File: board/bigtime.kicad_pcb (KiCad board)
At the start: 2 copper layers, 90 x 142 mm, 122 parts, among them IC1 NPIC6C596A, IC2 TPS62152, IC3 25AA02E48, IC4 STM32F407VET6, IC5 KSZ8081RNx, IC6 MAX5969x, IC7 MAX17503, IC8 LDL212DR, J1 RJHSE-538B, J2 MICROUSB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

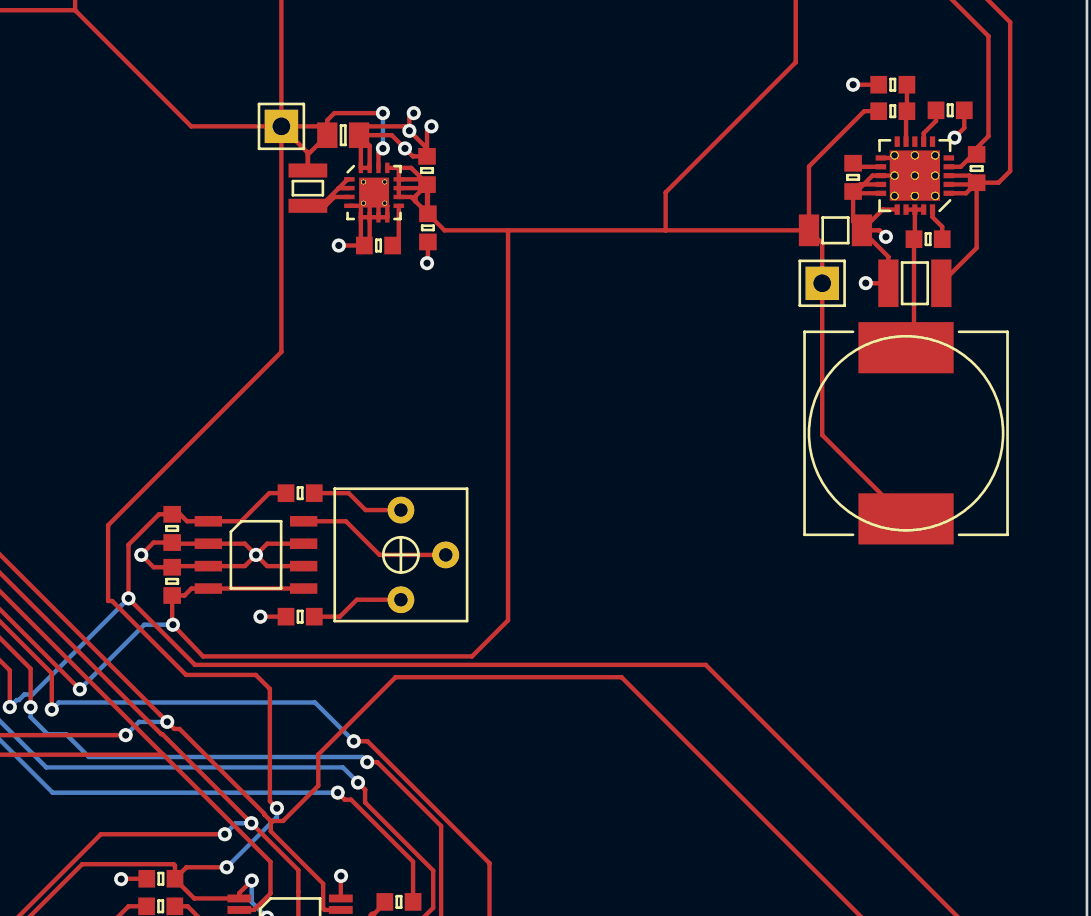
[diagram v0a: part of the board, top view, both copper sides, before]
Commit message: Tidied SMPS layouts
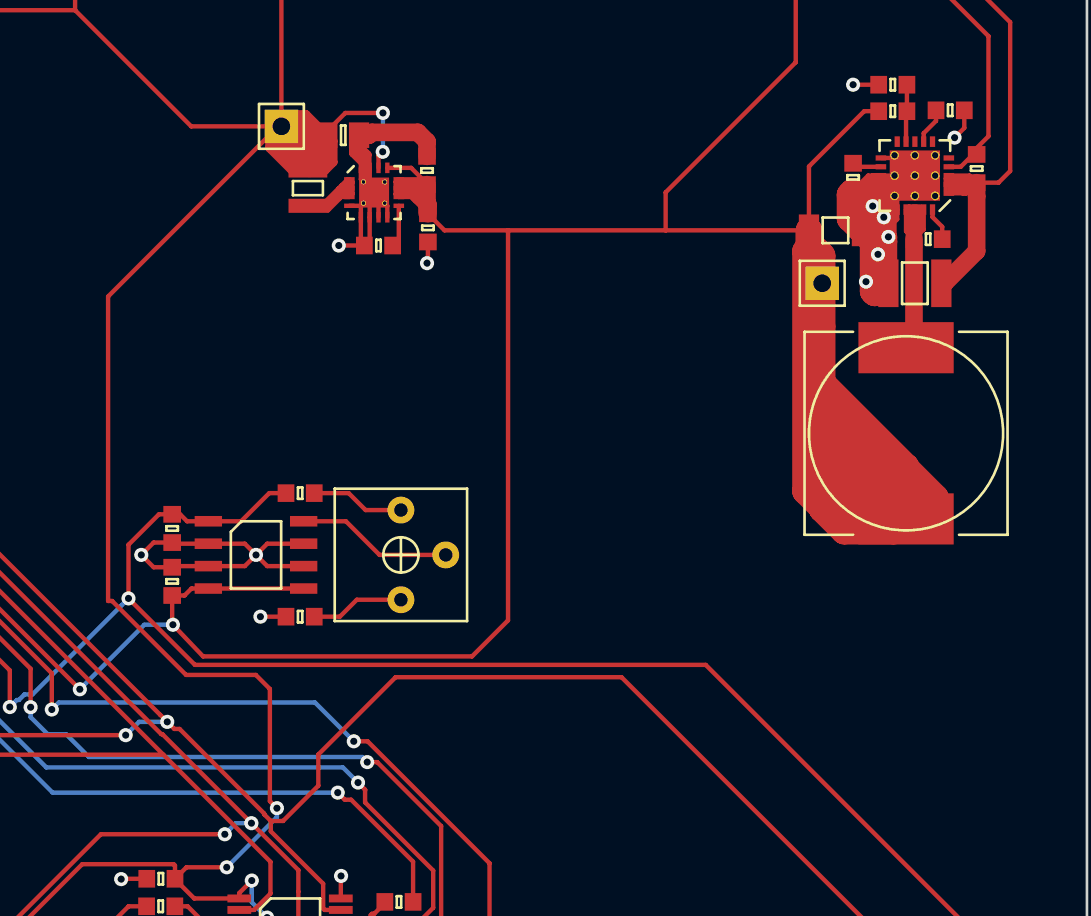
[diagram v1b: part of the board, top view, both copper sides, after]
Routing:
- net +12V: track 255.4 -> 314.3 mm
- net GND: track 155.6 -> 189.1 mm, vias 52 -> 51
- net +3V3: track 486.9 -> 500.6 mm
- net Net-(IC2-Pad1): track 6.13 -> 14.9 mm
- net Net-(C39-Pad2): track 9.03 -> 15.8 mm
- net +48V: track 82.6 -> 87.7 mm

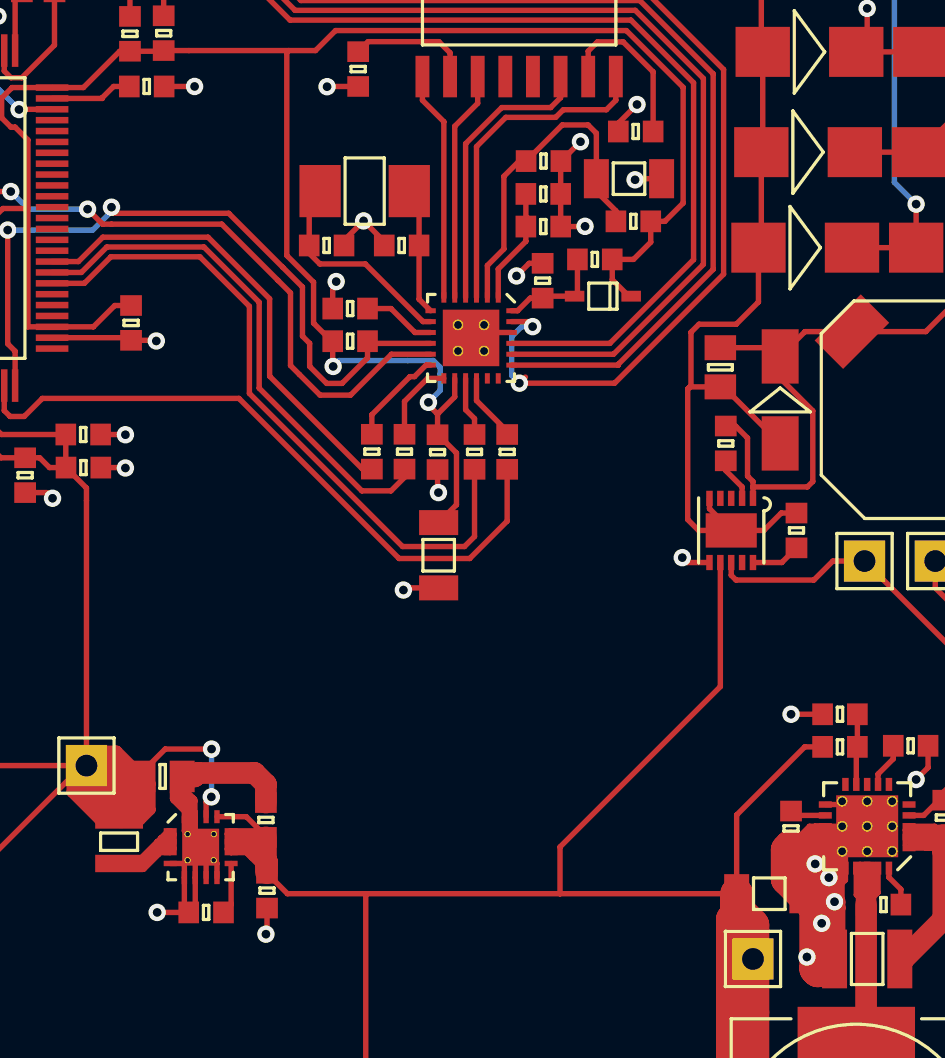
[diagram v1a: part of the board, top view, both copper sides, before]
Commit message: Made capacitors more consistent in vals+fps
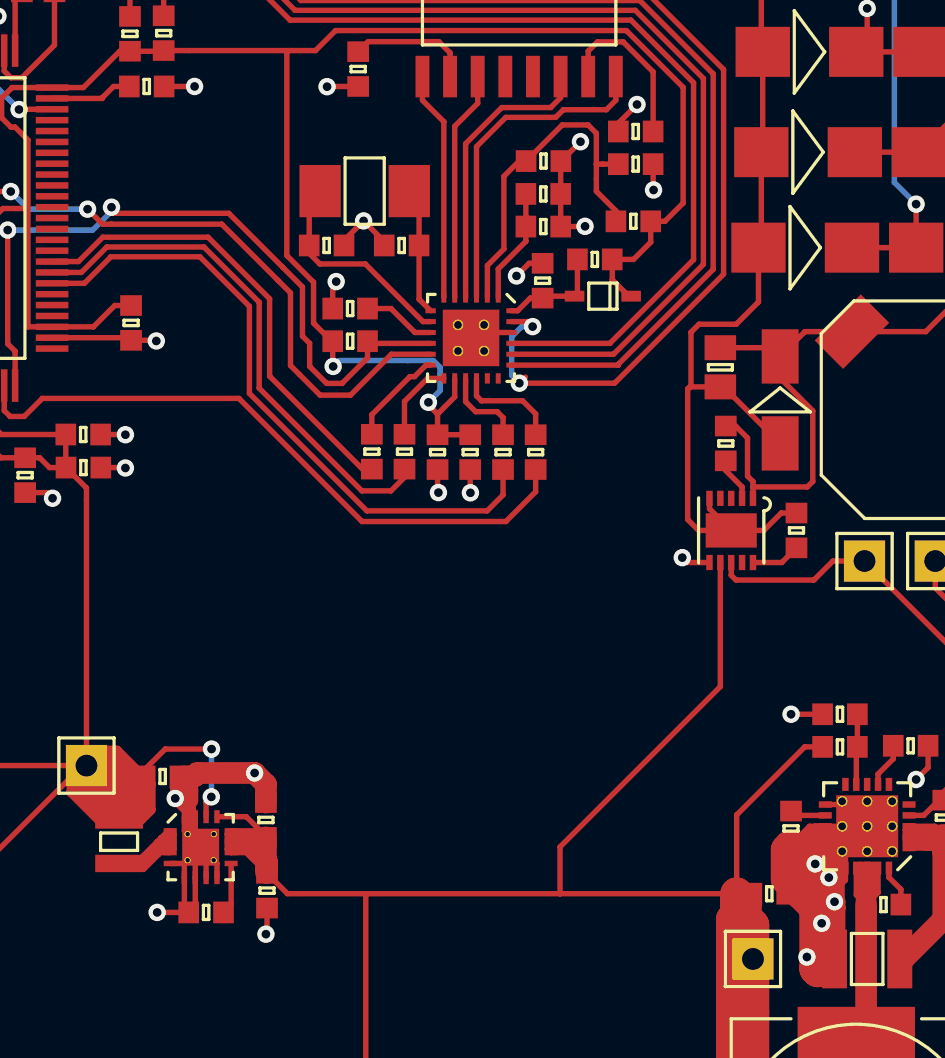
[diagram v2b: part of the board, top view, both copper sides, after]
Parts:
- C23, C25: footprint agg:1206 -> agg:0603
- C35: value C -> 10u
- C4: footprint agg:0805 -> agg:0603
- C41: value 2u -> 2u2; footprint agg:1206 -> agg:0603
- R24: value 3M3 -> 2M
- moved C25 4.96 mm to (187.0, 66.4)
- moved R13 1.31 mm to (188.5, 66.4)
- moved R14 1.31 mm to (190.0, 66.4)
- moved C23 0.74 mm to (194.6, 53.2)
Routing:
- net +3V3: track 500.6 -> 497.4 mm
- net +12V: track 314.3 -> 316.7 mm
- net Net-(IC5-Pad16): track 3.16 -> 4.82 mm
- net /RMII_CRS_DV: track 31.1 -> 29.9 mm
- net Net-(IC5-Pad15): track 2.75 -> 3.88 mm
- net Net-(C23-Pad1): track 15.9 -> 16.9 mm
- net GND: track 189.1 -> 190.1 mm, vias 51 -> 53
- net /RMII_REF_CLK: track 30.9 -> 30.0 mm

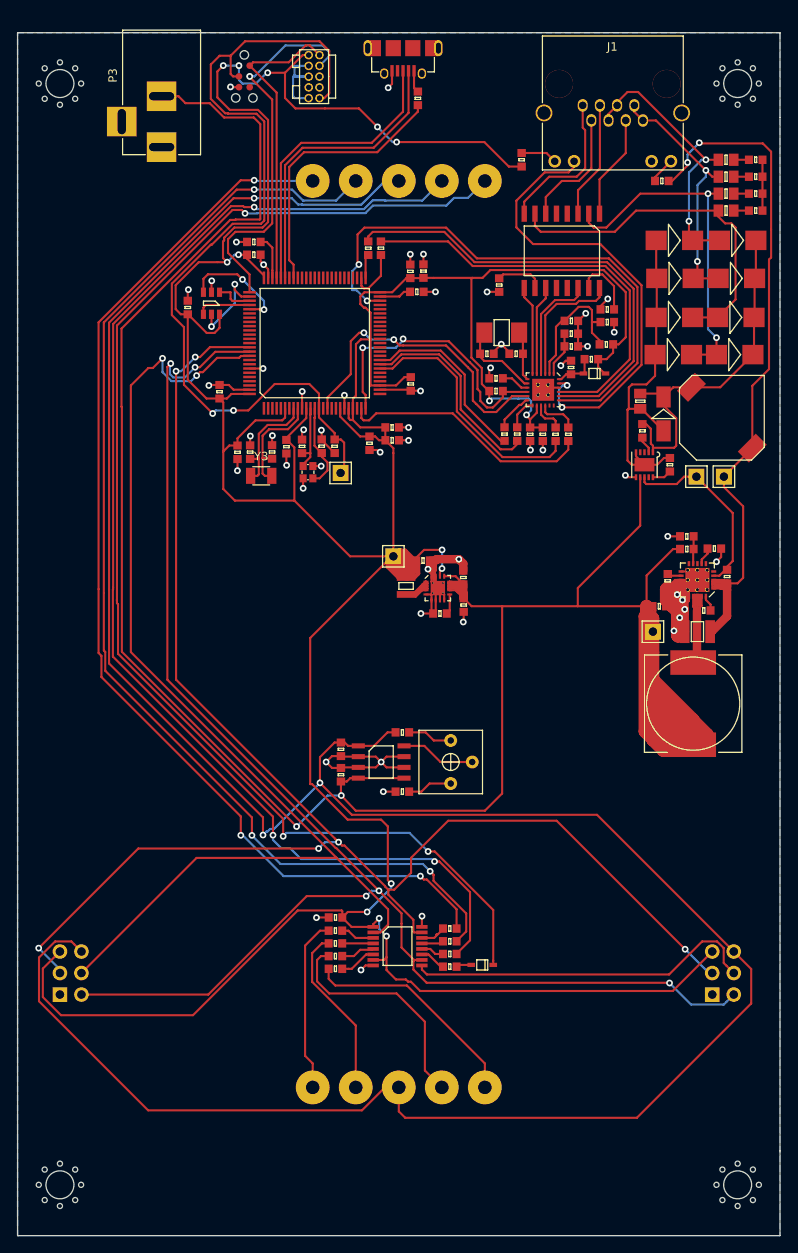
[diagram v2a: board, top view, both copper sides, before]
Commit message: Tidied top half of board
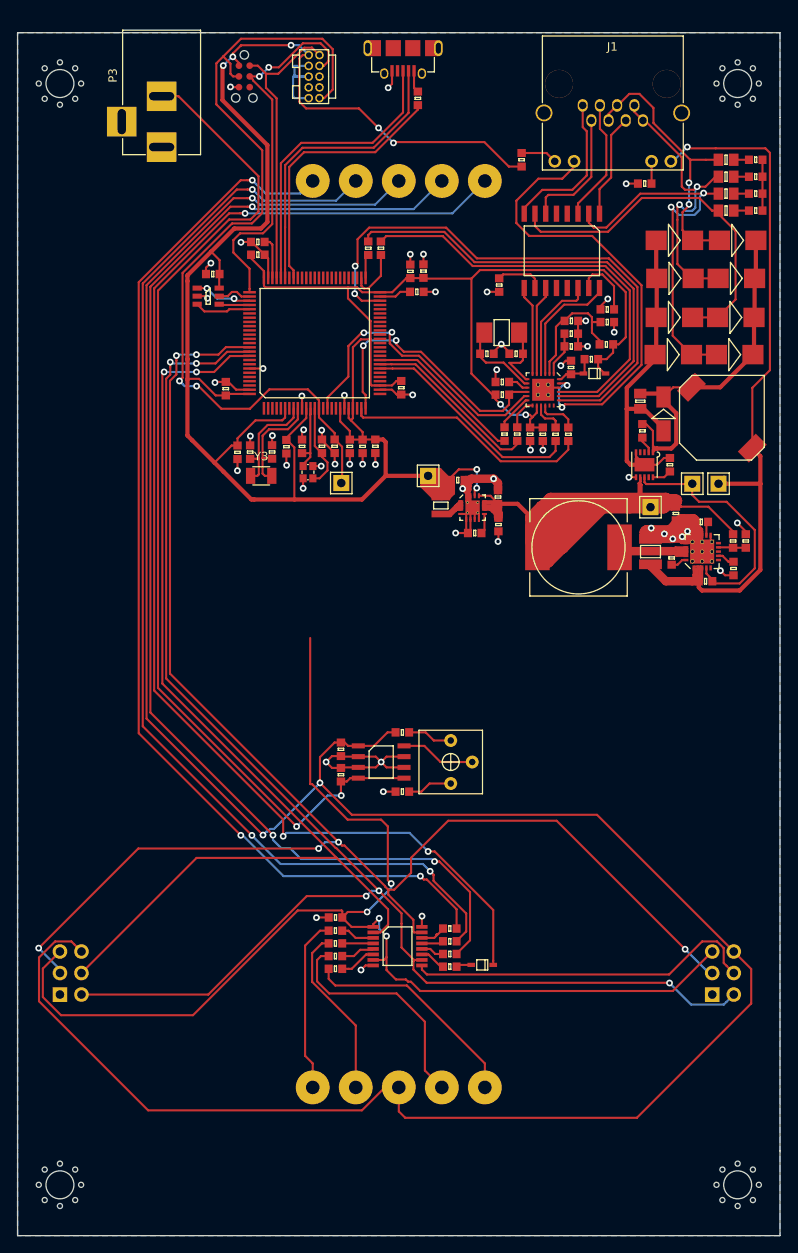
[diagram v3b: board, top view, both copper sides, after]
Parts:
- moved L4 22.9 mm to (191.2, 79.8), turned to 270 degrees
- moved TP4 14.7 mm to (199.7, 75.0), turned to 180 degrees
- moved C41 11.1 mm to (202.7, 75.8), turned to 270 degrees
- moved C38 11.0 mm to (199.7, 80.2), turned to 270 degrees
- moved C2 10.3 mm to (181.7, 73.8)
- moved C3 10.3 mm to (179.0, 78.1)
- moved C4 10.3 mm to (177.0, 71.8)
- moved C46 10.3 mm to (181.8, 77.1)
- moved IC2 10.3 mm to (178.7, 75.1)
- moved L1 10.3 mm to (175.0, 74.8)
- moved TP1 10.3 mm to (173.5, 71.3)
- moved C43 8.00 mm to (205.7, 76.8), turned to 180 degrees
- moved C39 7.27 mm to (202.2, 81.0), turned to 90 degrees
- moved R28 6.98 mm to (211.0, 79.0), turned to 90 degrees
- moved R27 5.54 mm to (209.5, 79.0), turned to 270 degrees
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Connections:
- J1 pad 11: GND -> Net-(J1-Pad11)
- J1 pad 12: Net-(J1-Pad12) -> +48V
- R18 pad 1: Net-(J1-Pad12) -> Net-(J1-Pad11)
- R18 pad 2: +48V -> GND
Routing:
- net +12V: track 316.7 -> 238.0 mm
- net +3V3: track 497.4 -> 479.1 mm, vias 15 -> 13
- net /DS_IN: track 132.8 -> 125.1 mm
- net /ethernet/POE_GOOD: track 22.1 -> 29.4 mm
- net /ROM_MOSI: track 13.3 -> 6.64 mm, vias 2 -> 0
- net +48V: track 87.7 -> 94.1 mm, vias 2 -> 1
- net /ROM_CS: track 10.3 -> 4.01 mm, vias 2 -> 0
- net /ethernet/VB1: track 31.0 -> 36.2 mm
- net /ethernet/VA1: track 40.8 -> 45.8 mm
- net /~RST: track 105.4 -> 101.2 mm
- net Net-(D1-Pad1): track 154.6 -> 150.5 mm
- net /LED_D: track 138.9 -> 135.1 mm
- net /LED_C: track 148.6 -> 144.9 mm
- net /V_LED_BUS: track 307.3 -> 303.7 mm
- net /RMII_CRS_DV: track 29.9 -> 26.5 mm
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
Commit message: Beefed 12V and V_LED_BUS
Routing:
- net +12V: track 238.0 -> 277.2 mm
- net +3V3: track 479.1 -> 489.2 mm, vias 13 -> 12
- net /V_LED_BUS: track 303.7 -> 304.8 mm
- net Net-(D1-Pad1): track 150.5 -> 151.5 mm
- net /LED_E: track 128.4 -> 127.5 mm
- net /LED_C: track 144.9 -> 145.6 mm

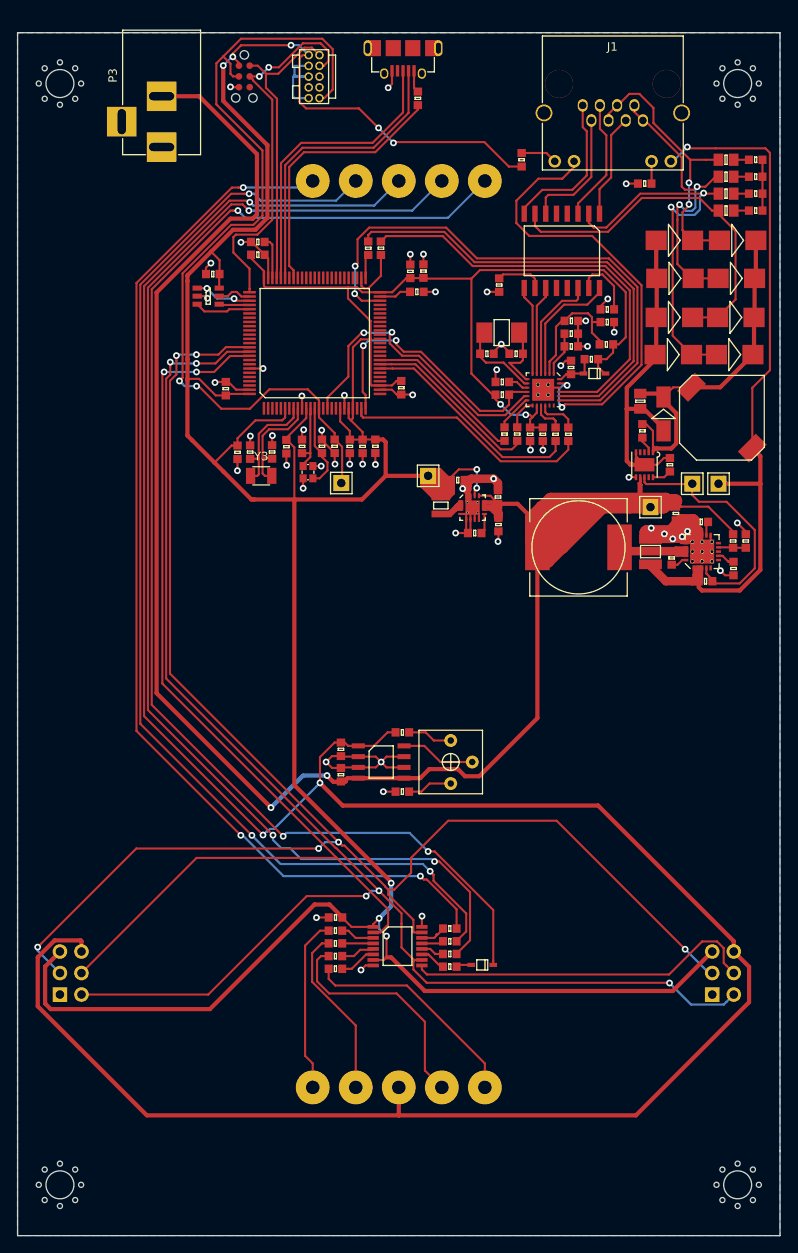
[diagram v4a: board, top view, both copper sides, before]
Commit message: Finished cleaning routing, rounded corners
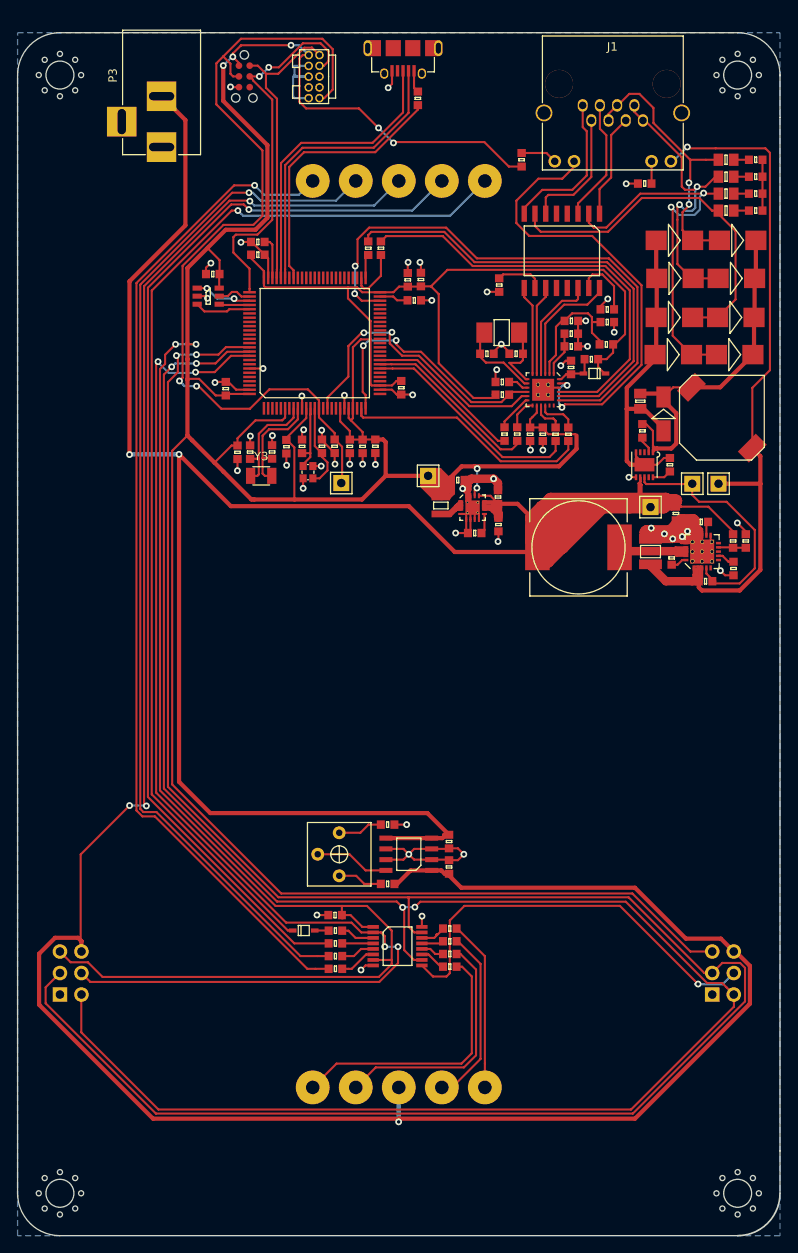
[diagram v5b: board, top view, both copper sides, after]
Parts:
- moved D1 21.5 mm to (158.8, 125.0), turned to 0 degrees
- moved C21 18.9 mm to (175.9, 117.5), turned to 90 degrees
- moved R2 18.0 mm to (168.7, 119.5), turned to 180 degrees
- moved RV1 17.1 mm to (163.0, 116.0), turned to 270 degrees
- moved C22 15.0 mm to (175.9, 114.5), turned to 90 degrees
- moved IC8 11.4 mm to (171.2, 116.0), turned to 180 degrees
- moved R3 4.26 mm to (168.7, 112.5), turned to 0 degrees
- moved C10 1.04 mm to (171.1, 48.2)
- moved C15 1.04 mm to (171.8, 50.6)
- moved C8 1.04 mm to (172.6, 48.1)
- moved X1 1.00 mm to (210.0, 156.0)
- moved X2 1.00 mm to (130.0, 24.0)
- moved X3 1.00 mm to (130.0, 156.0)
- moved X4 1.00 mm to (210.0, 24.0)
- moved C1 0.28 mm to (162.5, 123.2)
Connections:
- R1 pad 1: /LED_G -> /LED_DP
- R10 pad 1: /LED_E -> /LED_B
- R4 pad 1: /LED_F -> /LED_C
- R5 pad 1: /LED_A -> /LED_D
- R6 pad 1: /LED_B -> /LED_E
- R7 pad 1: /LED_DP -> /LED_G
- R8 pad 1: /LED_C -> /LED_F
- R9 pad 1: /LED_D -> /LED_A
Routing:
- net +3V3: track 489.2 -> 607.9 mm, vias 12 -> 9
- net /STCP: track 175.2 -> 237.4 mm, vias 5 -> 4
- net /SHCP: track 185.4 -> 246.1 mm, vias 6 -> 2
- net Net-(D1-Pad1): track 151.5 -> 127.9 mm, vias 3 -> 1
- net /V_LED_BUS: track 304.8 -> 282.3 mm, vias 3 -> 4
- net +12V: track 277.2 -> 297.2 mm
- net /LED_C: track 145.6 -> 129.2 mm, vias 3 -> 1
- net /DS_IN: track 125.1 -> 140.7 mm, vias 2 -> 4
- net /LED_D: track 135.0 -> 122.6 mm, vias 3 -> 1
- net /LED_G: track 20.6 -> 32.3 mm
- net /LED_F: track 20.4 -> 30.9 mm
- net /LED_E: track 127.5 -> 119.4 mm, vias 3 -> 1
- net /DS_OUT: track 41.7 -> 49.6 mm, vias 0 -> 1
- net /LED_A: track 27.4 -> 21.1 mm
- net /LED_B: track 26.6 -> 21.7 mm
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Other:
- outline, holes or cut-outs redrawn

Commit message: Final finishing touches and gerbers
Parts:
- added TP6: GND, agg:SIL-254P-01, F.Cu at (169.9, 156.0)
- added X5: PART, Symbols:Polarity_Center_Positive_6mm_SilkScreen, F.Cu at (137.9, 40.8)
- P1, P2: moved to F.Cu
- U1: value SA40-19 -> SA40-19SURKWA
- moved P1 8.01 mm to (138.0, 133.0)
- moved P2 3.04 mm to (204.0, 133.0)
- moved TP3 2.64 mm to (210.4, 72.1)
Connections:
- P3 pad 1: GND -> +12V
- P3 pad 2: +12V -> GND
- P3 pad 3: (no net) -> GND
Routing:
- net +3V3: track 607.9 -> 538.9 mm, vias 9 -> 10
- net +12V: track 297.2 -> 250.0 mm
- net GND: track 193.1 -> 182.1 mm, vias 54 -> 57
- net /STCP: track 237.4 -> 227.1 mm, vias 4 -> 2
- net /SHCP: track 246.1 -> 238.7 mm
- net /DS_OUT: track 49.6 -> 42.7 mm, vias 1 -> 0
- net /V_LED_BUS: track 282.3 -> 288.1 mm
- net /DS_IN: track 140.7 -> 138.1 mm, vias 4 -> 2
- net +48V: track 94.1 -> 91.5 mm
- net /RMII_MDIO: track 31.0 -> 28.8 mm, vias 2 -> 3
- net /RMII_MDC: track 35.4 -> 33.7 mm
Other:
- net class Default: clearance 0.2 -> 0.18
- rule trace_clearance: 0.2 -> 0.18
- board text added: "+12V"
- board text added: "+48V"
- board text added: "3v3"
- board text added: "BIGTIME"
- board text added: "David Turner 2017-03-31"
- board text added: "GND"
- board text added: "GND SHCP 3v3 STCP DATA V_LED"
- board text added: "IN"
- board text added: "LINK"
- board text added: "MAC:"
- board text added: "OUT"
- board text added: "PoE"
- board text added: "RESET"
- board text added: "david@dwt27.co.uk"
- board text added: "github.com/cillian64/bigtime"
- board text added: "r1"
